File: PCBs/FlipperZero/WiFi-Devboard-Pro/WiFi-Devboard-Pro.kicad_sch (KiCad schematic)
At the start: 35 parts

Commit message: import PCB dxf, schematics reviewed
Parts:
- gave numbers to parts that had none: 35

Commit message: Place components on PCB
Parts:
- added LED2: TX, LEDC1608X50N, symbol SamacSys_Parts:19-217_Y5C-AP1Q2_3T
- added LED3: RX, LEDC1608X50N, symbol SamacSys_Parts:19-217_Y5C-AP1Q2_3T
- added LED4: 3V3, 19217R6CAL1M2VY3T, symbol SamacSys_Parts:19-217_R6C-AL1M2VY_3T
- added R13, R14, R15: 1K, RESC1005X40N, symbol SamacSys_Parts:RC0402FR-071KL
- J4, J5: footprint (none) -> Connector_PinHeader_2.54mm:PinHeader_1x11_P2.54mm_Vertical
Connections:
- net +3V3: now also R13.1, R14.1, R15.1
- net GND: now also LED4.2
- net RX: now also LED2.1
- net TX: now also LED3.1
- new net: LED3.2, R14.2
- new net: LED2.2, R13.2
- new net: LED4.1, R15.2
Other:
- note added: "Status LEDs"

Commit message: Review done (#185)
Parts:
- added C10, C11, C7, C8, C9: 100n, CAPC1005X55N, symbol SamacSys_Parts:CL05B104KO5NNNC
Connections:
- net +3V3: now also C7.2; no longer J3.1 (Pin_1)
- net +5V: now also C9.2; no longer J2.1 (Pin_1)
- net +LDO_3V3: now also C10.2
- net +ext_3V3: now also J3.1 (Pin_1), C8.2
- net +ext_5V: now also J2.1 (Pin_1), C11.2
- net GND: now also C10.1, C11.1, C7.1, C8.1, C9.1
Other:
- note added: "ESP32"
- moved on the sheet: IC3, J6, R3, R4, R5

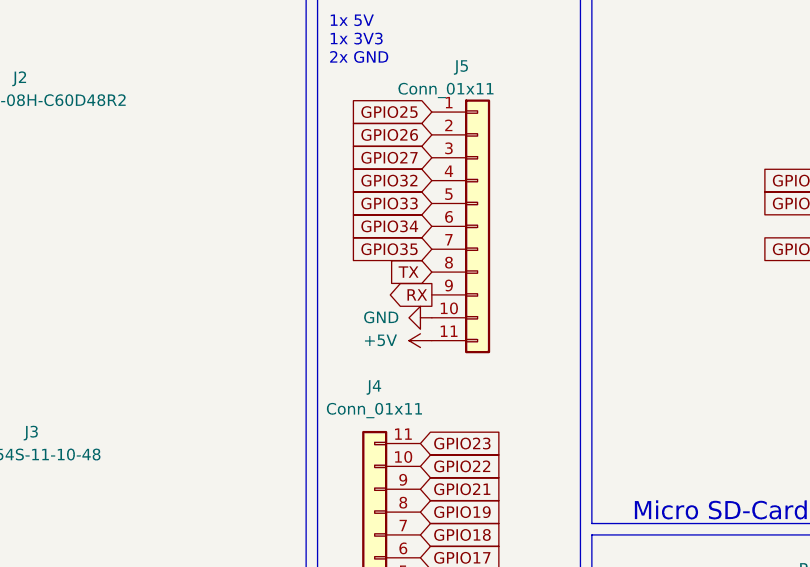
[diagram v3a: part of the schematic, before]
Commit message: preliminary review done, change RT and TX breakout, add PWR planes 3V3 and GND
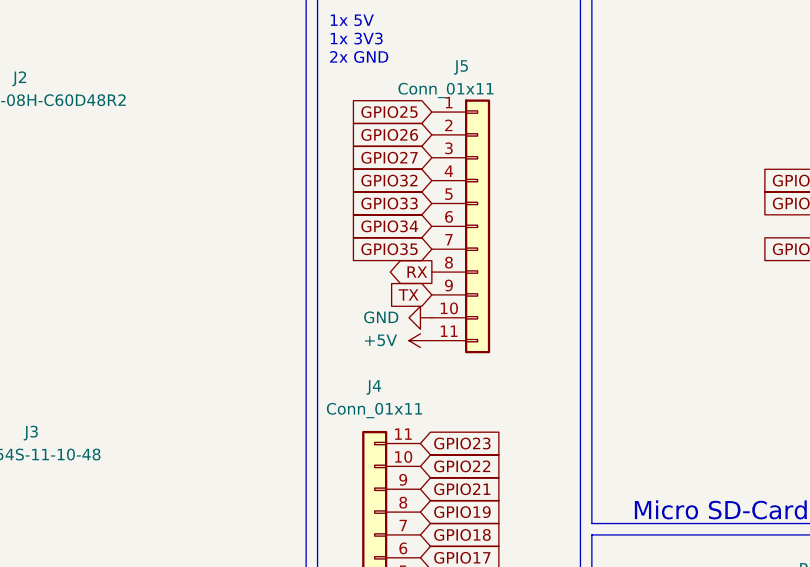
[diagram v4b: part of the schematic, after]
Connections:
- net RX: now also J5.8 (Pin_8); no longer J5.9 (Pin_9)
- net TX: now also J5.9 (Pin_9); no longer J5.8 (Pin_8)
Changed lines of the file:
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@@
     )
   )
-  (global_label "RX" (shape output) (at 109.22 185.42 180) (fields_autoplaced)
+  (global_label "RX" (shape output) (at 109.22 182.88 180) (fields_autoplaced)
     (effects (font (size 1.27 1.27)) (justify right))
-    (property "Intersheet References" "${INTERSHEET_REFS}" (id 0) (at 104.3274 185.4994 0)
+    (property "Intersheet References" "${INTERSHEET_REFS}" (id 0) (at 104.3274 182.9594 0)
       (effects (font (size 1.27 1.27)) (justify right) hide)
     )
@@
     )
   )
-  (global_label "TX" (shape input) (at 109.22 182.88 180) (fields_autoplaced)
+  (global_label "TX" (shape input) (at 109.22 185.42 180) (fields_autoplaced)
     (effects (font (size 1.27 1.27)) (justify right))
-    (property "Intersheet References" "${INTERSHEET_REFS}" (id 0) (at 104.6298 182.9594 0)
+    (property "Intersheet References" "${INTERSHEET_REFS}" (id 0) (at 104.6298 185.4994 0)
       (effects (font (size 1.27 1.27)) (justify right) hide)
     )

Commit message: More traces and plains
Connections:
- net +3V3: now also C4.2, LED1.4 (VDD)
- net +5V: no longer C4.2, LED1.4 (VDD)
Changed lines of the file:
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@@
     (pin "2")
-  )
-  (symbol (lib_id "power:+5V") (at 160.02 234.95 180) (unit 1)
-    (in_bom yes) (on_board yes) (fields_autoplaced)
-    (property "Reference" "#PWR019" (id 0) (at 160.02 231.14 0)
-      (effects (font (size 1.27 1.27)) hide)
-    )
-    (property "Value" "+5V" (id 1) (at 162.56 236.2199 0)
-      (effects (font (size 1.27 1.27)) (justify right))
-    )
-    (property "Footprint" "" (id 2) (at 160.02 234.95 0)
-      (effects (font (size 1.27 1.27)) hide)
-    )
-    (property "Datasheet" "" (id 3) (at 160.02 234.95 0)
-      (effects (font (size 1.27 1.27)) hide)
-    )
-    (pin "1")
   )
   (symbol (lib_id "SamacSys_Parts:DMP1045U-7") (at 422.91 102.87 90) (unit 1)
@@
     (pin "1")
     (pin "2")
+  )
+  (symbol (lib_id "power:+3V3") (at 160.02 234.95 180) (unit 1)
+    (in_bom yes) (on_board yes) (fields_autoplaced)
+    (property "Reference" "#PWR?" (id 0) (at 160.02 231.14 0)
+      (effects (font (size 1.27 1.27)) hide)
+    )
+    (property "Value" "+3V3" (id 1) (at 162.56 236.2199 0)
+      (effects (font (size 1.27 1.27)) (justify right))
+    )
+    (property "Footprint" "" (id 2) (at 160.02 234.95 0)
+      (effects (font (size 1.27 1.27)) hide)
+    )
+    (property "Datasheet" "" (id 3) (at 160.02 234.95 0)
+      (effects (font (size 1.27 1.27)) hide)
+    )
+    (pin "1")
   )
   (symbol (lib_id "power:GND") (at 138.43 232.41 270) (unit 1)
@@
       (reference "#PWR018") (unit 1) (value "GND") (footprint "")
     )
-    (path "/8ed88628-5c3f-4ae7-9b4b-beb883cfb4f0"
-      (reference "#PWR019") (unit 1) (value "+5V") (footprint "")
-    )
     (path "/fb4a82ab-fad5-4134-bb57-c6e9036e7754"
       (reference "#PWR020") (unit 1) (value "GND") (footprint "")
@@
       (reference "#PWR0102") (unit 1) (value "+ext_3V3") (footprint "")
     )
+    (path "/d3edf629-33c1-45ba-9af4-caa80199d7c4"
+      (reference "#PWR?") (unit 1) (value "+3V3") (footprint "")
+    )
     (path "/40adbb6d-87aa-405c-ba38-fc70c2bcc5dc"

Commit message: started review
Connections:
- net +3V3: now also J4.2 (Pin_2); no longer J4.1 (Pin_1)
- net +5V: now also J5.2 (Pin_2); no longer J5.11 (Pin_11)
- net GND: now also J4.1 (Pin_1), J5.1 (Pin_1); no longer J4.2 (Pin_2), J5.10 (Pin_10)
- net GPIO25: now also J5.3 (Pin_3); no longer J5.1 (Pin_1)
- net GPIO26: now also J5.4 (Pin_4); no longer J5.2 (Pin_2)
- net GPIO27: now also J5.5 (Pin_5); no longer J5.3 (Pin_3)
- net GPIO32: now also J5.6 (Pin_6); no longer J5.4 (Pin_4)
- net GPIO33: now also J5.7 (Pin_7); no longer J5.5 (Pin_5)
- net GPIO34: now also J5.8 (Pin_8); no longer J5.6 (Pin_6)
- net GPIO35: now also J5.9 (Pin_9); no longer J5.7 (Pin_7)
- net RX: now also J5.10 (Pin_10); no longer J5.8 (Pin_8)
- net TX: now also J5.11 (Pin_11); no longer J5.9 (Pin_9)

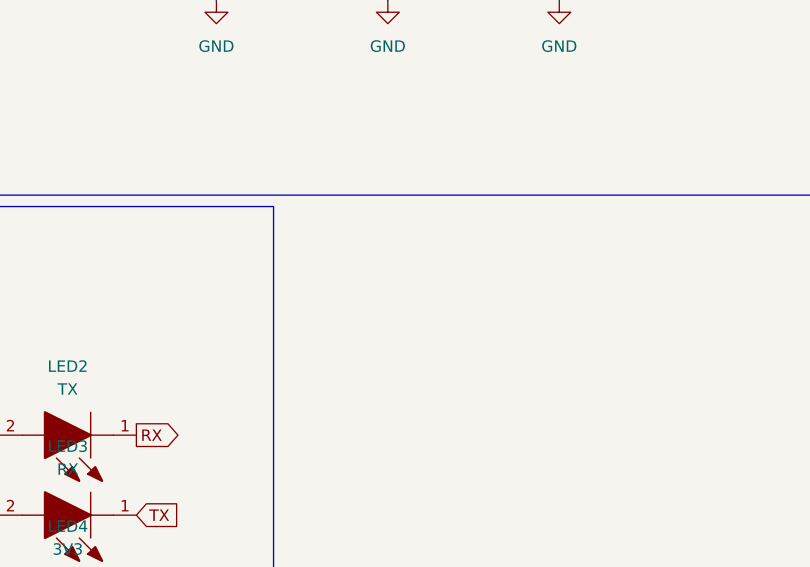
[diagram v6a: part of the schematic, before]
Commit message: Stream review, add logo and text
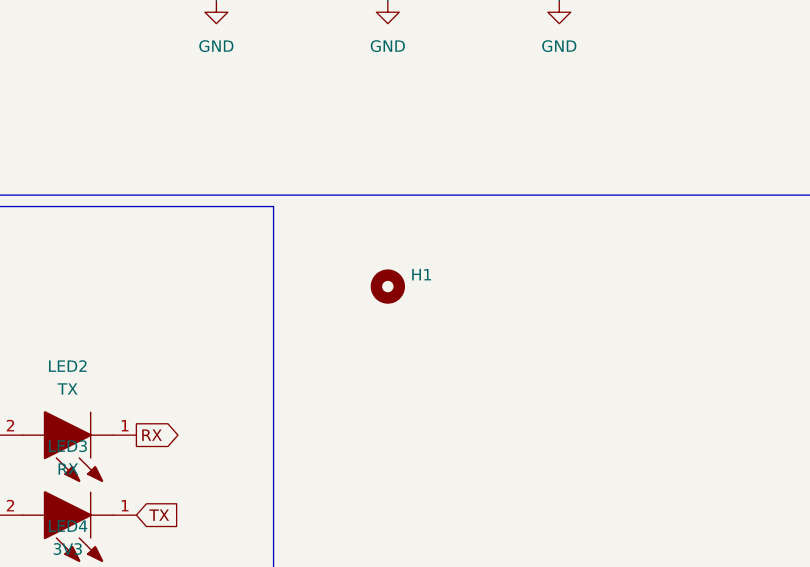
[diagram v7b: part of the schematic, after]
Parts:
- added H1: (no value), symbol Mechanical:MountingHole
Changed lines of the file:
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@@
     (pin "1")
+  )
+  (symbol (lib_id "Mechanical:MountingHole") (at 355.6 187.96 0) (unit 1)
+    (in_bom yes) (on_board yes) (fields_autoplaced)
+    (property "Reference" "H1" (id 0) (at 358.14 186.6899 0)
+      (effects (font (size 1.27 1.27)) (justify left))
+    )
+    (property "Value" "" (id 1) (at 358.14 189.2299 0)
+      (effects (font (size 1.27 1.27)) (justify left))
+    )
+    (property "Footprint" "" (id 2) (at 355.6 187.96 0)
+      (effects (font (size 1.27 1.27)) hide)
+    )
+    (property "Datasheet" "~" (id 3) (at 355.6 187.96 0)
+      (effects (font (size 1.27 1.27)) hide)
+    )
   )
   (symbol (lib_id "power:GND") (at 176.53 198.12 0) (unit 1)
@@
   (symbol (lib_id "power:+3V3") (at 107.95 224.79 270) (unit 1)
     (in_bom yes) (on_board yes) (fields_autoplaced)
-    (property "Reference" "#PWR?" (id 0) (at 104.14 224.79 0)
+    (property "Reference" "#PWR01" (id 0) (at 104.14 224.79 0)
       (effects (font (size 1.27 1.27)) hide)
     )
@@
   (symbol (lib_id "power:GND") (at 107.95 227.33 90) (unit 1)
     (in_bom yes) (on_board yes)
-    (property "Reference" "#PWR?" (id 0) (at 114.3 227.33 0)
+    (property "Reference" "#PWR03" (id 0) (at 114.3 227.33 0)
       (effects (font (size 1.27 1.27)) hide)
     )
@@
   (symbol (lib_id "power:+3V3") (at 160.02 234.95 180) (unit 1)
     (in_bom yes) (on_board yes) (fields_autoplaced)
-    (property "Reference" "#PWR?" (id 0) (at 160.02 231.14 0)
+    (property "Reference" "#PWR010" (id 0) (at 160.02 231.14 0)
       (effects (font (size 1.27 1.27)) hide)
     )
@@
   )
   (symbol_instances
+    (path "/873b26cb-57d8-496a-ba6d-014c367acc65"
+      (reference "#PWR01") (unit 1) (value "+3V3") (footprint "")
+    )
     (path "/fb596e4c-6b9f-4b73-8d91-d86ee0192628"
       (reference "#PWR02") (unit 1) (value "GND") (footprint "")
     )
+    (path "/cd0ef08e-1e0a-463d-934f-188987274c87"
+      (reference "#PWR03") (unit 1) (value "GND") (footprint "")
+    )
     (path "/d89013f9-d116-49ba-99c6-65da9c27ad5e"
       (reference "#PWR04") (unit 1) (value "GND") (footprint "")
@@
       (reference "#PWR09") (unit 1) (value "GND") (footprint "")
     )
+    (path "/d3edf629-33c1-45ba-9af4-caa80199d7c4"
+      (reference "#PWR010") (unit 1) (value "+3V3") (footprint "")
+    )
     (path "/b0228299-0eb8-4913-914c-6bb8874973f2"
       (reference "#PWR012") (unit 1) (value "GND") (footprint "")
@@
       (reference "#PWR0102") (unit 1) (value "+ext_3V3") (footprint "")
     )
-    (path "/873b26cb-57d8-496a-ba6d-014c367acc65"
-      (reference "#PWR?") (unit 1) (value "+3V3") (footprint "")
-    )
-    (path "/cd0ef08e-1e0a-463d-934f-188987274c87"
-      (reference "#PWR?") (unit 1) (value "GND") (footprint "")
-    )
-    (path "/d3edf629-33c1-45ba-9af4-caa80199d7c4"
-      (reference "#PWR?") (unit 1) (value "+3V3") (footprint "")
-    )
     (path "/40adbb6d-87aa-405c-ba38-fc70c2bcc5dc"
       (reference "C1") (unit 1) (value "1u") (footprint "CAPC1005X60N")
@@
       (reference "C11") (unit 1) (value "100n") (footprint "CAPC1005X55N")
     )
+    (path "/26d34c7a-663c-44ce-bf5d-9011a0023f0c"
+      (reference "H1") (unit 1) (value "MountingHole") (footprint "")
+    )
     (path "/7756c211-5286-4d10-828b-c4ad5bcfbce7"

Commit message: Update BOM
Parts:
- C1: footprint CAPC1005X60N -> 0402; Comment (none) -> C1; LCSC Part Number (none) -> C14445
- C10, C11, C3, C7, C8, C9: footprint CAPC1005X55N -> 0402; Comment (none) -> C3,C7,C8,C9,C10,C11; LCSC Part Number (none) -> C1525
- C2, C5: footprint CAPC1005X80N -> 0402; Comment (none) -> C2,C5; LCSC Part Number (none) -> C919306
- C4: footprint CAPC1005X55N -> 0402; Comment (none) -> C4; LCSC Part Number (none) -> C1525
- C6: footprint CAPC1005X70N -> 0402; Comment (none) -> C6; LCSC Part Number (none) -> C15525
- H1: value (none) -> MountingHole; Comment (none) -> H1
- IC1: footprint ESP32WROOM32EN4 -> SMD-38P,18x25.5x3.1mm; Comment (none) -> IC1; LCSC Part Number (none) -> C701341
- IC2, IC4, IC5: footprint SOT96P240X120-3N -> SOT-23; Comment (none) -> IC2,IC4,IC5; LCSC Part Number (none) -> C177033
- IC3: footprint SOT230P700X180-4N -> SOT-223-3; Comment (none) -> IC3; LCSC Part Number (none) -> C92517
- J1: Comment (none) -> J1
- J2: footprint HUSRSP8W66P254_2000X250X850P -> SMD,P=2.54mm(交错脚); Comment (none) -> J2; LCSC Part Number (none) -> C2883765
- J3: Comment (none) -> J3; LCSC Part Number (none) -> C5160793
- J4, J5: footprint Connector_PinHeader_2.54mm:PinHeader_1x11_P2.54mm_Vertical -> SMD,P=2.54mm(交错脚); Comment (none) -> J4,J5
- J6: footprint 503398-1892 -> SMD; Comment (none) -> J6; LCSC Part Number (none) -> C428492
- LED1: Comment (none) -> LED1; LCSC Part Number (none) -> C965555
- LED2: footprint LEDC1608X50N -> 0603; Comment (none) -> LED2; LCSC Part Number (none) -> C434424
- LED3: footprint LEDC1608X50N -> 0603; Comment (none) -> LED3; LCSC Part Number (none) -> C434424
- LED4: footprint 19217R6CAL1M2VY3T -> 0603; Comment (none) -> LED4; LCSC Part Number (none) -> C84263
- R1, R6: footprint RESC1005X40N -> 0402; Comment (none) -> R1,R6; LCSC Part Number (none) -> C60490
- R10, R11, R12, R7, R8, R9: footprint RESC1005X40N -> 0402; Comment (none) -> R7,R8,R9,R10,R11,R12; LCSC Part Number (none) -> C60491
- R13, R14, R15, R3, R4, R5: footprint RESC1005X40N -> 0402; Comment (none) -> R3,R4,R5,R13,R14,R15; LCSC Part Number (none) -> C106235
- R2: footprint RESC1005X40N -> 0402; Comment (none) -> R2; LCSC Part Number (none) -> C25091
- S1, S2: footprint SKRPABE010 -> SMD; Comment (none) -> S1,S2; LCSC Part Number (none) -> C115360
- U1, U2, U3: Comment (none) -> U1,U2,U3; LCSC Part Number (none) -> C460232
